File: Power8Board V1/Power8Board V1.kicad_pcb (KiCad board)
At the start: 2 copper layers, 100 x 100 mm, 87 parts, among them J0 XT30, J1 XT30, J10 XT60IPW-M, J2 XT30, J3 XT30, J4 XT30, J5 XT30, J6 XT30, J7 XT30, J8 Qwiic_RA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

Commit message: There is a general layout.
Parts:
- removed C6: 56 uF, PCR1J560MCL1GS:CAP_PC_8X12_NCH
- added J9: MR30PW-M, Connector_AMASS:AMASS_MR30PW-M_1x03_P3.50mm_Horizontal, F.Cu at (118.0, 106.0)
- moved J10 302.9 mm to (178.5, 100.2), turned to -90 degrees
- moved J8 290.7 mm to (181.8, 46.7)
- moved U1 278.1 mm to (181.2, 103.0), turned to -90 degrees
- moved R19 251.7 mm to (129.5, 137.5), turned to 90 degrees
- moved R13 249.4 mm to (129.5, 91.2), turned to 90 degrees
- moved C33 247.0 mm to (121.7, 134.5), turned to 180 degrees
- moved R14 246.4 mm to (129.5, 68.0), turned to 90 degrees
- moved C27 246.3 mm to (121.7, 88.0), turned to 180 degrees
- moved C28 244.3 mm to (121.7, 64.8), turned to 180 degrees
- moved U11 242.9 mm to (121.5, 137.5), turned to 180 degrees
- moved U5 239.9 mm to (121.5, 91.2), turned to 180 degrees
- moved C4 239.1 mm to (190.0, 117.8), turned to 90 degrees
- moved C2 237.7 mm to (189.5, 88.5), turned to 90 degrees
- moved U6 236.7 mm to (121.5, 68.0), turned to 180 degrees
- moved C18 229.1 mm to (163.5, 68.1), turned to 90 degrees
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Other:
- outline, holes or cut-outs redrawn
- board text added: "CHECK PINS"

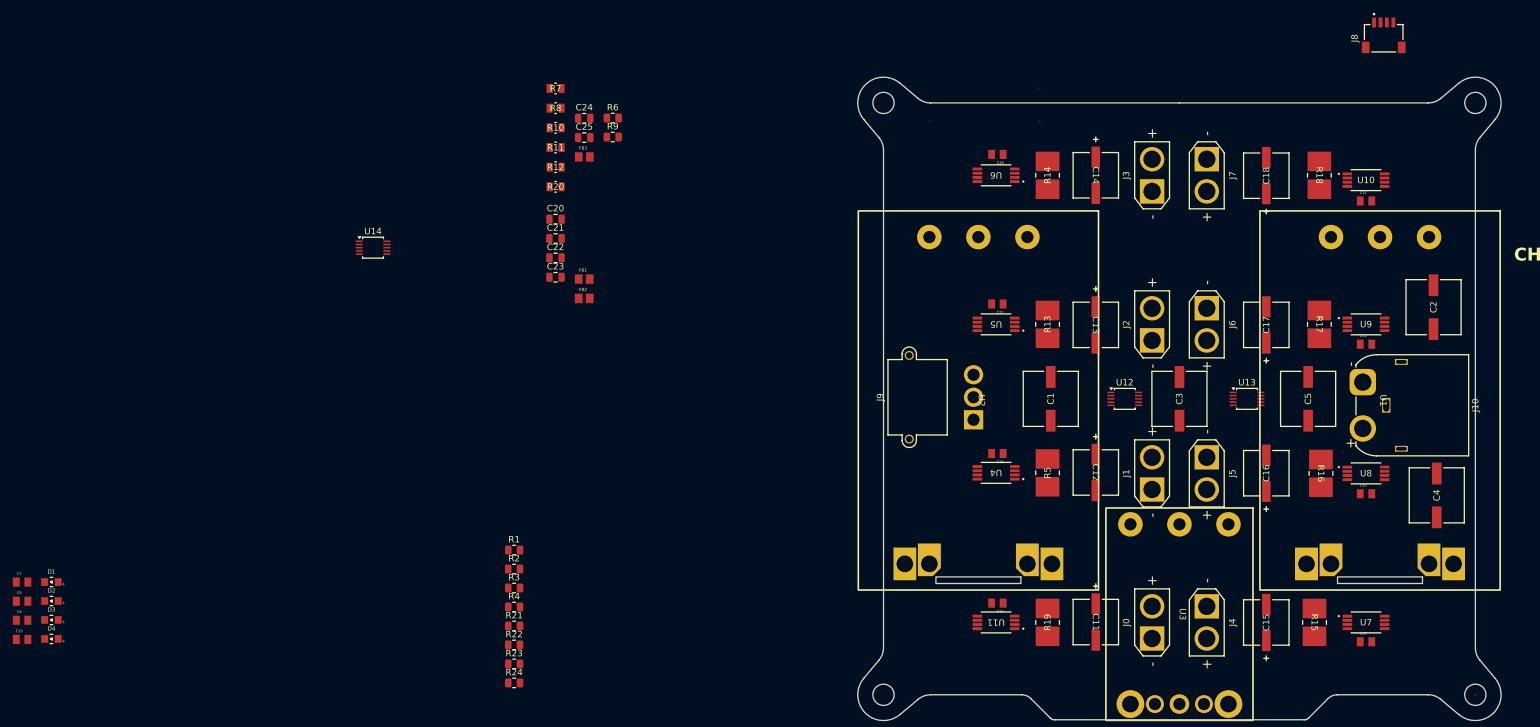
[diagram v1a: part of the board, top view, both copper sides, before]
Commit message: Laid out components
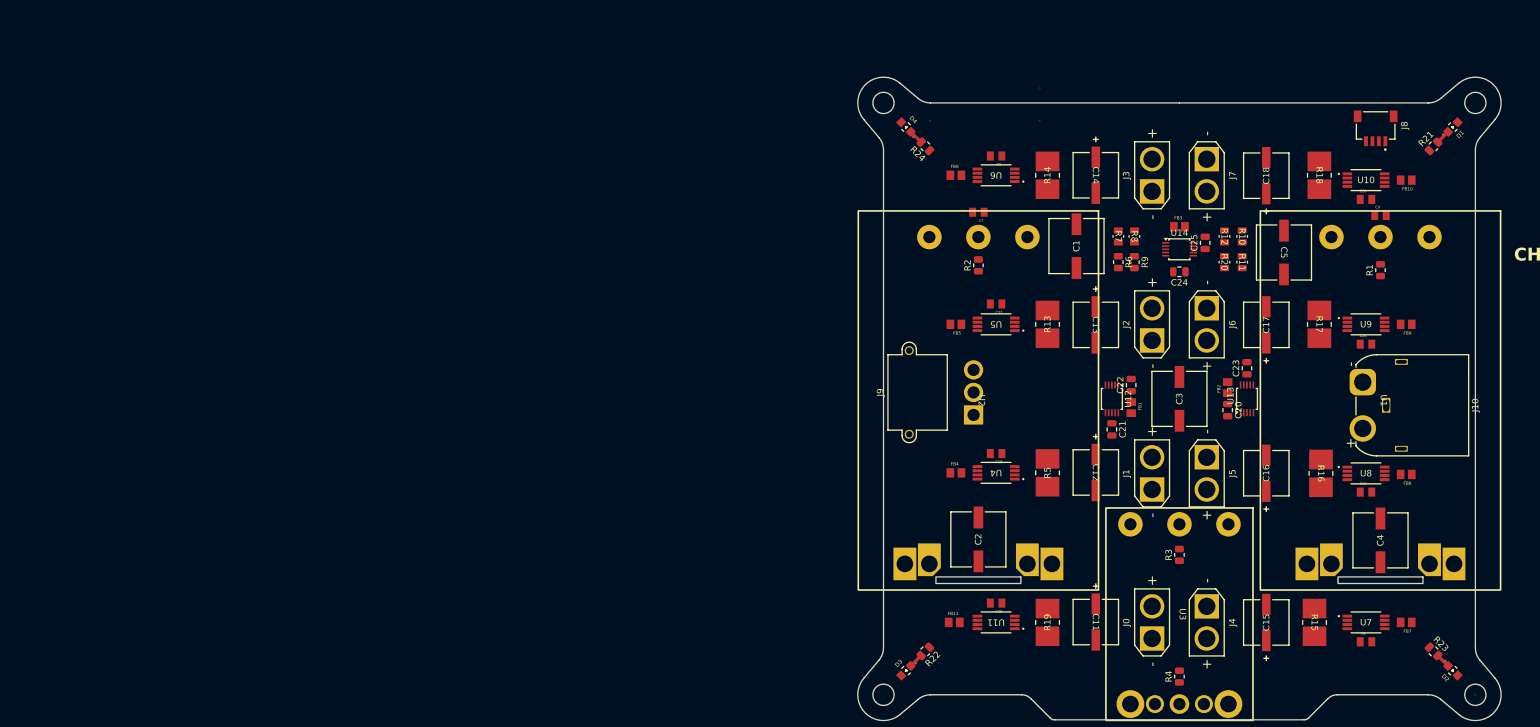
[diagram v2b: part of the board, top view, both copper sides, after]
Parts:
- removed C30, C31, C32, C33: 0.1 uF, 0805 Ceramic Capacitor:CAPC2012X140N
- added C26: 0.1 uF, 0805 Ceramic Capacitor:CAPC2012X140N, F.Cu at (179.0, 94.2)
- added C6: 0.1 uF, 0805 Ceramic Capacitor:CAPC2012X140N, F.Cu at (121.5, 65.0)
- added FB10: FerriteBead, MPZ2012S102ATD25:BEADC2012X105N, F.Cu at (185.2, 68.8)
- added FB11: FerriteBead, MPZ2012S102ATD25:BEADC2012X105N, F.Cu at (115.0, 137.5)
- added FB4: FerriteBead, MPZ2012S102ATD25:BEADC2012X105N, F.Cu at (115.2, 114.2)
- added FB5: FerriteBead, MPZ2012S102ATD25:BEADC2012X105N, F.Cu at (115.2, 91.2)
- added FB6: FerriteBead, MPZ2012S102ATD25:BEADC2012X105N, F.Cu at (115.2, 68.0)
- added FB7: FerriteBead, MPZ2012S102ATD25:BEADC2012X105N, F.Cu at (185.2, 137.5)
- added FB8: FerriteBead, MPZ2012S102ATD25:BEADC2012X105N, F.Cu at (185.2, 114.5)
- added FB9: FerriteBead, MPZ2012S102ATD25:BEADC2012X105N, F.Cu at (185.2, 91.2)
- moved D1 229.0 mm to (192.5, 60.5), turned to -135 degrees
- moved C9 220.3 mm to (181.2, 74.2)
- moved D2 218.1 mm to (192.5, 145.0), turned to 135 degrees
- moved C10 210.1 mm to (179.0, 117.2)
- moved C8 209.0 mm to (179.0, 140.5)
- moved R21 161.2 mm to (189.5, 63.5), turned to 45 degrees
- moved C7 159.4 mm to (118.8, 73.8), turned to 180 degrees
- moved D4 154.8 mm to (107.5, 60.5), turned to -45 degrees
- moved R23 142.9 mm to (189.5, 142.0), turned to -45 degrees
- moved R1 141.5 mm to (181.2, 82.8), turned to 90 degrees
- moved D3 133.1 mm to (107.5, 145.0), turned to 45 degrees
- moved U14 125.4 mm to (150.0, 79.5)
- moved C20 108.6 mm to (157.5, 104.5), turned to -90 degrees
- moved C23 108.4 mm to (160.5, 98.0), turned to 90 degrees
- moved R11 108.2 mm to (159.8, 81.5), turned to -90 degrees
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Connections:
- C10 pad 2: +48V -> +3.3VA/8
- C19 pad 2: +3.3V -> +3.3VA/4
- C27 pad 2: +3.3V -> +3.3VA/5
- C28 pad 2: +3.3V -> +3.3VA/10
- C29 pad 2: +3.3V -> +3.3VA/11
- C8 pad 2: +48V -> +3.3VA/7
- U10 pad 5: +3.3V -> +3.3VA/10
- U11 pad 5: +3.3V -> +3.3VA/11
- U13 pad 1: +3.3V -> +3.3VA/2
- U4 pad 5: +3.3V -> +3.3VA/4
- U5 pad 5: +3.3V -> +3.3VA/5
- U6 pad 5: +3.3V -> +3.3VA/6
- U7 pad 5: +3.3V -> +3.3VA/7
- U8 pad 5: +3.3V -> +3.3VA/8
- U9 pad 5: +3.3V -> +3.3VA/9
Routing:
- net Net-(D3-A): track 0.00 -> 2.29 mm
- net Net-(D4-A): track 0.00 -> 2.28 mm
- net Net-(D2-A): track 0.00 -> 2.28 mm
- net Net-(D1-A): track 0.00 -> 2.28 mm

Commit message: Laying out 9/5.
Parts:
- added C30: 56 uF, PCR1J560MCL1GS:CAP_PC_8X12_NCH, F.Cu at (5.44, 4.48)
- moved C1 56.7 mm to (82.5, 102.8), turned to -90 degrees
- moved C5 24.1 mm to (170.2, 103.8), turned to 90 degrees
- moved C21 2.93 mm to (138.5, 104.8), turned to 180 degrees
- moved C23 2.69 mm to (161.5, 100.5), turned to 0 degrees
- moved C22 2.20 mm to (142.5, 98.4)
- moved FB1 2.20 mm to (142.5, 101.9)
- moved U12 2.20 mm to (139.5, 100.6)
- moved C20 1.75 mm to (157.5, 106.2)
- moved FB2 1.75 mm to (157.5, 102.8)
- moved U13 1.75 mm to (160.5, 104.5)
- moved R16 1.50 mm to (170.5, 114.3)
- moved R17 1.25 mm to (170.5, 91.2)
- moved R18 1.25 mm to (170.5, 68.0)
- moved C28 0.75 mm to (179.0, 71.0)
- moved FB10 0.75 mm to (185.2, 68.0)
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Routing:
- net GND: track 0.00 -> 58.0 mm, vias 0 -> 14
- net +12V: track 0.00 -> 27.8 mm
- net +12V/0: track 0.00 -> 6.94 mm
- net +12V/3: track 0.00 -> 6.94 mm
- net +12V/1: track 0.00 -> 6.94 mm
- net +12V/2: track 0.00 -> 6.84 mm
- net +3.3VA/11: track 0.00 -> 6.00 mm
- net +3.3VA/5: track 0.00 -> 5.92 mm
- net +3.3VA/4: track 0.00 -> 5.83 mm
- net +3.3VA/6: track 0.00 -> 5.75 mm
- net +3.3V: vias 0 -> 4
- added copper zone on F.Cu, net +12V
- added copper zone on F.Cu, net +12V/0
- added copper zone on F.Cu, net +12V/1
- added copper zone on F.Cu, net +12V/2
- added copper zone on F.Cu, net +12V/3
- added copper zone on In2.Cu, net +3.3V
- added copper zone on In1.Cu, net GND
- added copper zone on In4.Cu, net GND
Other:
- outline, holes or cut-outs redrawn
- copper layers 2 -> 6

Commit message: About half a side is done.
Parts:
- moved C21 6.50 mm to (138.6, 98.2)
- moved C22 4.85 mm to (142.8, 103.2), turned to -90 degrees
- moved FB1 2.28 mm to (142.8, 99.6), turned to 90 degrees
- moved U12 1.85 mm to (139.5, 102.4), turned to 90 degrees
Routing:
- net +5V: track 0.00 -> 112.8 mm, vias 0 -> 1
- net +3.3V: track 0.00 -> 56.5 mm, vias 4 -> 12
- net /Current Sensing/INA240 Current Sensor 0/OUT0: track 0.00 -> 47.4 mm, vias 0 -> 2
- net /Current Sensing/INA240 Current Sensor 3/OUT3: track 0.00 -> 42.6 mm, vias 0 -> 2
- net /Current Sensing/INA240 Current Sensor 2/OUT2: track 0.00 -> 28.7 mm, vias 0 -> 2
- net /Current Sensing/INA240 Current Sensor 1/OUT1: track 0.00 -> 27.7 mm, vias 0 -> 2
- net +3.3VA/1: track 0.00 -> 5.47 mm
- net GND: track 58.0 -> 61.8 mm, vias 14 -> 19
- net +3.3VA/2: track 0.00 -> 3.63 mm
- net Net-(U3-Trim): track 0.00 -> 2.93 mm
- added copper zone on In3.Cu, net +12V
- added copper zone on In3.Cu, net +48V

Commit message: Switched out input capacitors.
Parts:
- removed C30, C4, C5: 56 uF, PCR1J560MCL1GS:CAP_PC_8X12_NCH
- C1, C2, C3: value 56 uF -> 100 uF; footprint PCR1J560MCL1GS:CAP_PC_8X12_NCH -> 107AVG063MFBJ:CAP_AVG-8x12_ILC
- moved C1 88.3 mm to (170.8, 105.5), turned to 90 degrees
- moved C2 40.5 mm to (111.2, 84.8), turned to 0 degrees
- moved C3 34.7 mm to (179.5, 84.5), turned to 0 degrees
- moved R1 4.90 mm to (185.4, 80.1), turned to 135 degrees
- moved R2 1.00 mm to (119.8, 82.0), turned to 180 degrees

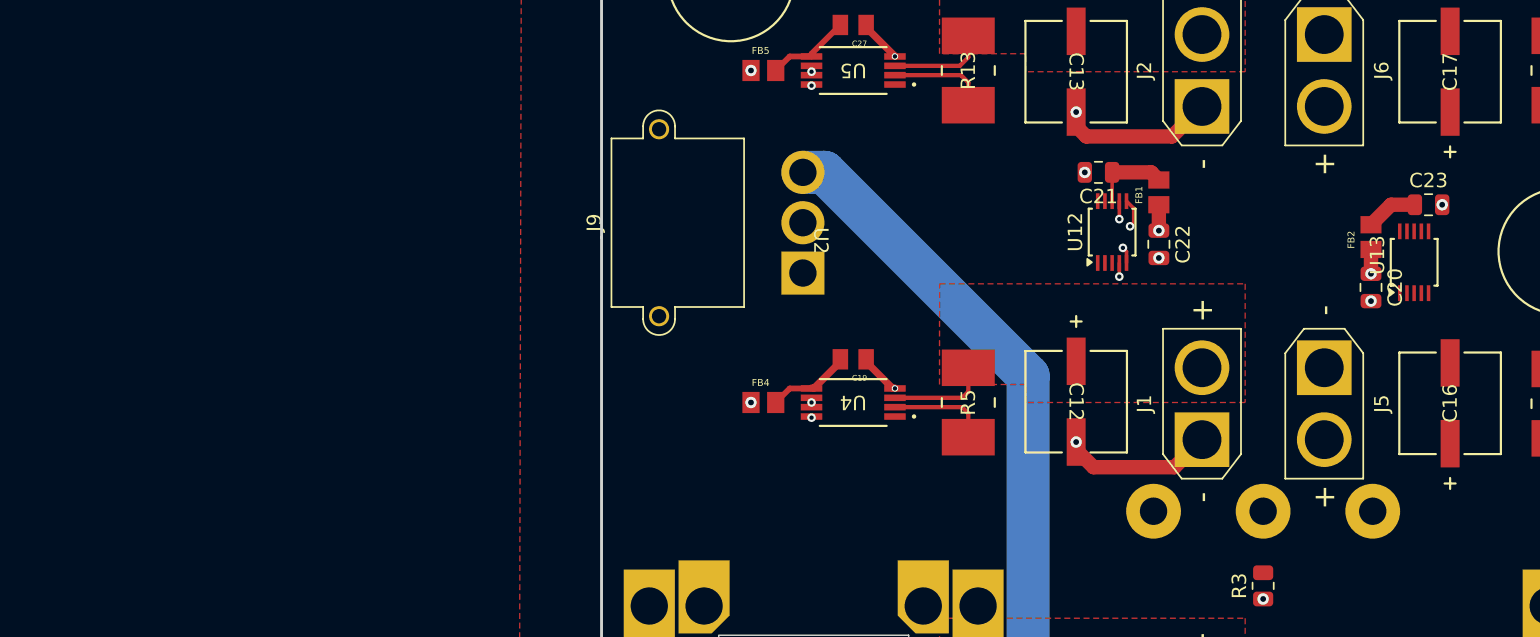
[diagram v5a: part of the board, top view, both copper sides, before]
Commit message: Added 0603 components and RC filters.
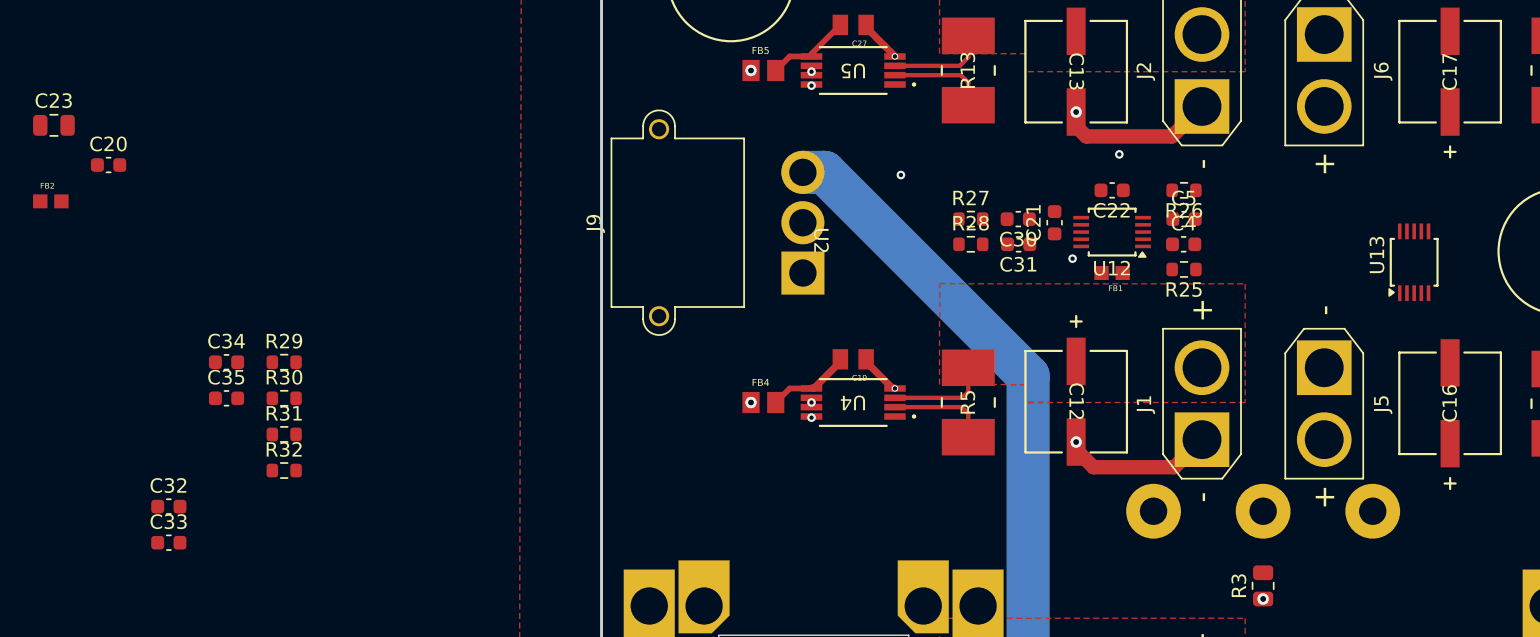
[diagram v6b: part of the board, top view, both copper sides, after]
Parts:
- added C30: 2.2 uF, Capacitor_SMD:C_0603_1608Metric, F.Cu at (133.0, 101.5)
- added C31: 2.2 uF, Capacitor_SMD:C_0603_1608Metric, F.Cu at (133.0, 103.2)
- added C32: 2.2 uF, Capacitor_SMD:C_0603_1608Metric, F.Cu at (73.9, 121.5)
- added C33: 2.2 uF, Capacitor_SMD:C_0603_1608Metric, F.Cu at (73.9, 124.0)
- added C34: 2.2 uF, Capacitor_SMD:C_0603_1608Metric, F.Cu at (77.9, 111.5)
- added C35: 2.2 uF, Capacitor_SMD:C_0603_1608Metric, F.Cu at (77.9, 114.0)
- added C4: 2.2 uF, Capacitor_SMD:C_0603_1608Metric, F.Cu at (144.5, 103.2)
- added C5: 2.2 uF, Capacitor_SMD:C_0603_1608Metric, F.Cu at (144.5, 101.5)
- added R25: 680, Resistor_SMD:R_0603_1608Metric, F.Cu at (144.5, 105.0)
- added R26: 680, Resistor_SMD:R_0603_1608Metric, F.Cu at (144.5, 99.5)
- added R27: 680, Resistor_SMD:R_0603_1608Metric, F.Cu at (129.7, 101.5)
- added R28: 680, Resistor_SMD:R_0603_1608Metric, F.Cu at (129.7, 103.2)
- added R29: 680, Resistor_SMD:R_0603_1608Metric, F.Cu at (81.9, 111.5)
- added R30: 680, Resistor_SMD:R_0603_1608Metric, F.Cu at (81.9, 114.0)
- added R31: 680, Resistor_SMD:R_0603_1608Metric, F.Cu at (81.9, 116.5)
- added R32: 680, Resistor_SMD:R_0603_1608Metric, F.Cu at (81.9, 119.0)
- C20, C21, C22: footprint Capacitor_SMD:C_0805_2012Metric -> Capacitor_SMD:C_0603_1608Metric
- FB1, FB2: footprint MPZ2012S102ATD25:BEADC2012X105N -> 0603 Ferrite Bead:0603 Ferrite Bead
- moved C23 95.7 mm to (65.9, 95.0)
- moved FB2 91.8 mm to (65.7, 100.3), turned to 0 degrees
- moved C20 88.2 mm to (69.7, 97.7), turned to 0 degrees
- moved FB1 6.48 mm to (139.5, 105.2), turned to 180 degrees
- moved C22 4.96 mm to (139.5, 99.5), turned to 180 degrees
- moved C21 4.64 mm to (135.5, 101.8), turned to 90 degrees
- turned U12 to 180 degrees
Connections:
- U12 pad 4: /Current Sensing/INA240 Current Sensor 0/OUT0 -> Net-(U12-AIN0)
- U12 pad 5: /Current Sensing/INA240 Current Sensor 1/OUT1 -> Net-(U12-AIN1)
- U12 pad 6: /Current Sensing/INA240 Current Sensor 2/OUT2 -> Net-(U12-AIN2)
- U12 pad 7: /Current Sensing/INA240 Current Sensor 3/OUT3 -> Net-(U12-AIN3)
- U13 pad 4: /Current Sensing/INA240 Current Sensor 4/OUT4 -> Net-(U13-AIN0)
- U13 pad 5: /Current Sensing/INA240 Current Sensor 5/OUT5 -> Net-(U13-AIN1)
- U13 pad 6: /Current Sensing/INA240 Current Sensor 6/OUT6 -> Net-(U13-AIN2)
- U13 pad 7: /Current Sensing/INA240 Current Sensor 7/OUT7 -> Net-(U13-AIN3)
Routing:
- net /Current Sensing/INA240 Current Sensor 2/OUT2: track 28.7 -> 8.79 mm
- net +3.3V: track 56.5 -> 41.1 mm, vias 12 -> 10
- net /Current Sensing/INA240 Current Sensor 3/OUT3: track 42.6 -> 36.8 mm
- net +3.3VA/1: track 5.47 -> 0.00 mm
- net +3.3VA/2: track 3.63 -> 0.00 mm
- net /Current Sensing/INA240 Current Sensor 1/OUT1: track 27.7 -> 24.3 mm
- net /Current Sensing/INA240 Current Sensor 0/OUT0: track 47.4 -> 46.4 mm, vias 2 -> 1
- net GND: vias 19 -> 15

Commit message: 9/22 Progress
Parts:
- C23: footprint Capacitor_SMD:C_0805_2012Metric -> Capacitor_SMD:C_0603_1608Metric
- moved C23 96.5 mm to (162.0, 103.5), turned to 90 degrees
- moved FB2 92.8 mm to (158.2, 107.0)
- moved C20 88.6 mm to (158.2, 101.2)
- moved R32 87.4 mm to (168.0, 103.5)
- moved C35 87.4 mm to (164.7, 103.5)
- moved C34 87.0 mm to (164.7, 105.2)
- moved R31 86.8 mm to (168.0, 105.2)
- moved C33 81.3 mm to (153.0, 105.2), turned to 180 degrees
- moved C32 81.1 mm to (153.0, 103.5), turned to 180 degrees
- moved R29 71.7 mm to (153.0, 101.8)
- moved R30 71.4 mm to (153.0, 107.0)
- moved J8 5.39 mm to (178.5, 55.2)
- moved C1 5.28 mm to (176.0, 106.1)
- moved J10 5.10 mm to (183.6, 100.2)
- moved J9 4.50 mm to (113.5, 105.2)
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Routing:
- net /Current Sensing/INA240 Current Sensor 7/OUT7: track 0.00 -> 42.7 mm, vias 0 -> 2
- net GND: track 61.8 -> 91.9 mm, vias 15 -> 44
- net /Current Sensing/INA240 Current Sensor 6/OUT6: track 0.00 -> 21.6 mm, vias 0 -> 2
- net +12V: track 27.8 -> 48.6 mm
- net +3.3VA/2: track 0.00 -> 18.9 mm, vias 0 -> 2
- net +48V: track 0.00 -> 16.6 mm, vias 0 -> 1
- net /Current Sensing/INA240 Current Sensor 1/OUT1: track 24.3 -> 36.0 mm
- net Net-(U12-AIN3): track 0.00 -> 10.3 mm, vias 0 -> 3
- net Net-(U13-AIN3): track 0.00 -> 10.2 mm, vias 0 -> 2
- net Net-(U13-AIN2): track 0.00 -> 9.92 mm, vias 0 -> 2
- net Net-(U12-AIN2): track 0.00 -> 9.21 mm, vias 0 -> 2
- net +3.3VA/1: track 0.00 -> 7.07 mm
- net +12V/7: track 0.00 -> 6.94 mm
- net /Current Sensing/INA240 Current Sensor 2/OUT2: track 8.79 -> 15.7 mm
- net +12V/6: track 0.00 -> 6.89 mm
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- added copper zone on F.Cu, net +12V/4
- added copper zone on F.Cu, net +12V/5
- added copper zone on F.Cu, net +12V/6
- added copper zone on F.Cu, net +12V/7
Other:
- board size 100 x 100 mm -> 217.4 x 102.2 mm
- board text added: "PIN RECEPTACLES"

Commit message: 9/23 Progress
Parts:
- moved C25 2.00 mm to (154.0, 80.5), turned to -90 degrees
- moved C20 0.75 mm to (159.0, 101.2)
- moved C21 0.75 mm to (137.2, 100.8)
- moved C22 0.75 mm to (141.2, 98.6)
- moved C23 0.75 mm to (162.8, 103.5)
- moved C30 0.75 mm to (134.2, 100.6)
- moved C31 0.75 mm to (134.2, 102.3)
- moved C32 0.75 mm to (153.8, 103.5)
- moved C33 0.75 mm to (153.8, 105.2)
- moved C34 0.75 mm to (165.5, 105.2)
- moved C35 0.75 mm to (165.5, 103.5)
- moved C4 0.75 mm to (146.2, 102.3)
- moved C5 0.75 mm to (146.2, 100.6)
- moved FB1 0.75 mm to (141.2, 104.5)
- moved FB2 0.75 mm to (159.0, 107.0)
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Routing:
- net SDA: track 0.86 -> 127.4 mm, vias 1 -> 5
- net SCL: track 0.08 -> 117.4 mm, vias 1 -> 4
- net /Current Sensing/INA240 Current Sensor 4/OUT4: track 0.00 -> 57.1 mm, vias 1 -> 2
- net +5V: track 112.4 -> 167.7 mm, vias 1 -> 3
- net +3.3V: track 45.8 -> 94.5 mm, vias 14 -> 15
- net GND: track 91.9 -> 139.0 mm, vias 44 -> 55
- net /Current Sensing/INA240 Current Sensor 5/OUT5: track 0.00 -> 31.2 mm, vias 1 -> 2
- net /Voltage Sensing/AIN2: track 0.00 -> 10.5 mm, vias 0 -> 2
- net /Voltage Sensing/AIN0: track 0.00 -> 10.3 mm, vias 0 -> 2
- net +3.3VA/3: track 0.00 -> 7.66 mm
- net /Voltage Sensing/AIN1: track 0.00 -> 7.63 mm, vias 0 -> 2
- net /Voltage Sensing/AIN3: track 0.00 -> 7.57 mm
- net +12V/4: track 0.00 -> 6.94 mm
- net +12V: track 48.6 -> 55.5 mm
- net +3.3VA/7: track 0.00 -> 5.86 mm
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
